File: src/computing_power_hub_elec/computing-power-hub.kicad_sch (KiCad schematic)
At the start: 0 parts

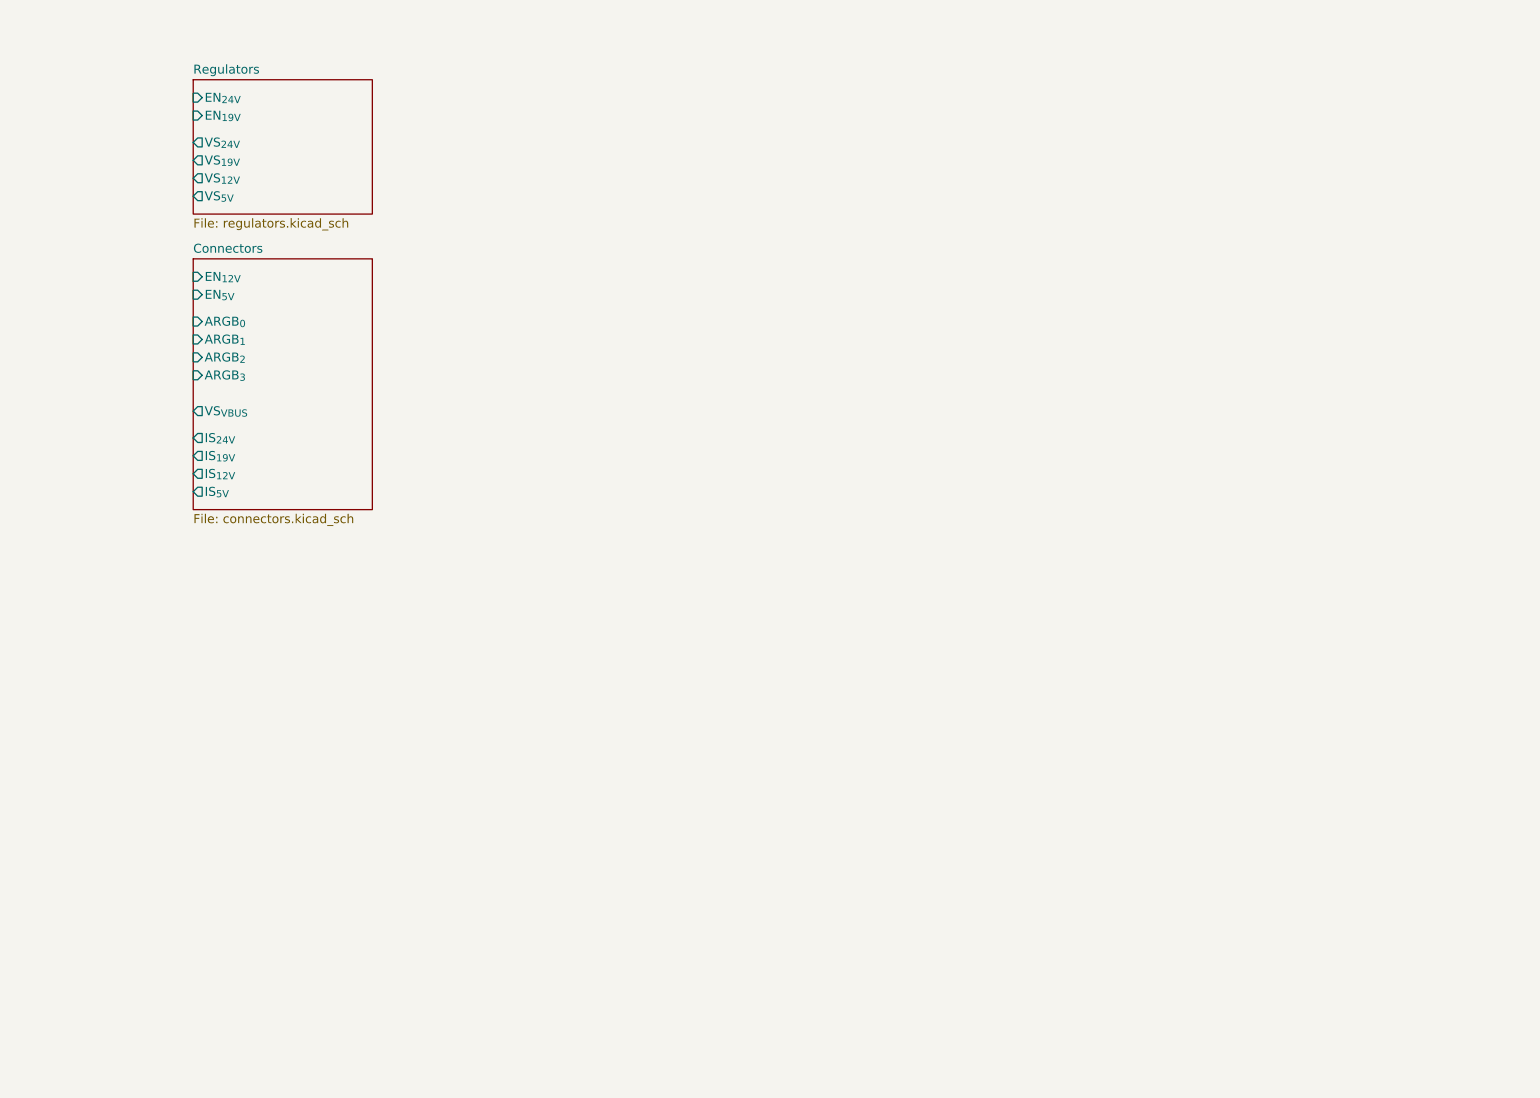
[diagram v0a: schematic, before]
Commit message: Complete first draft of compute power schematic
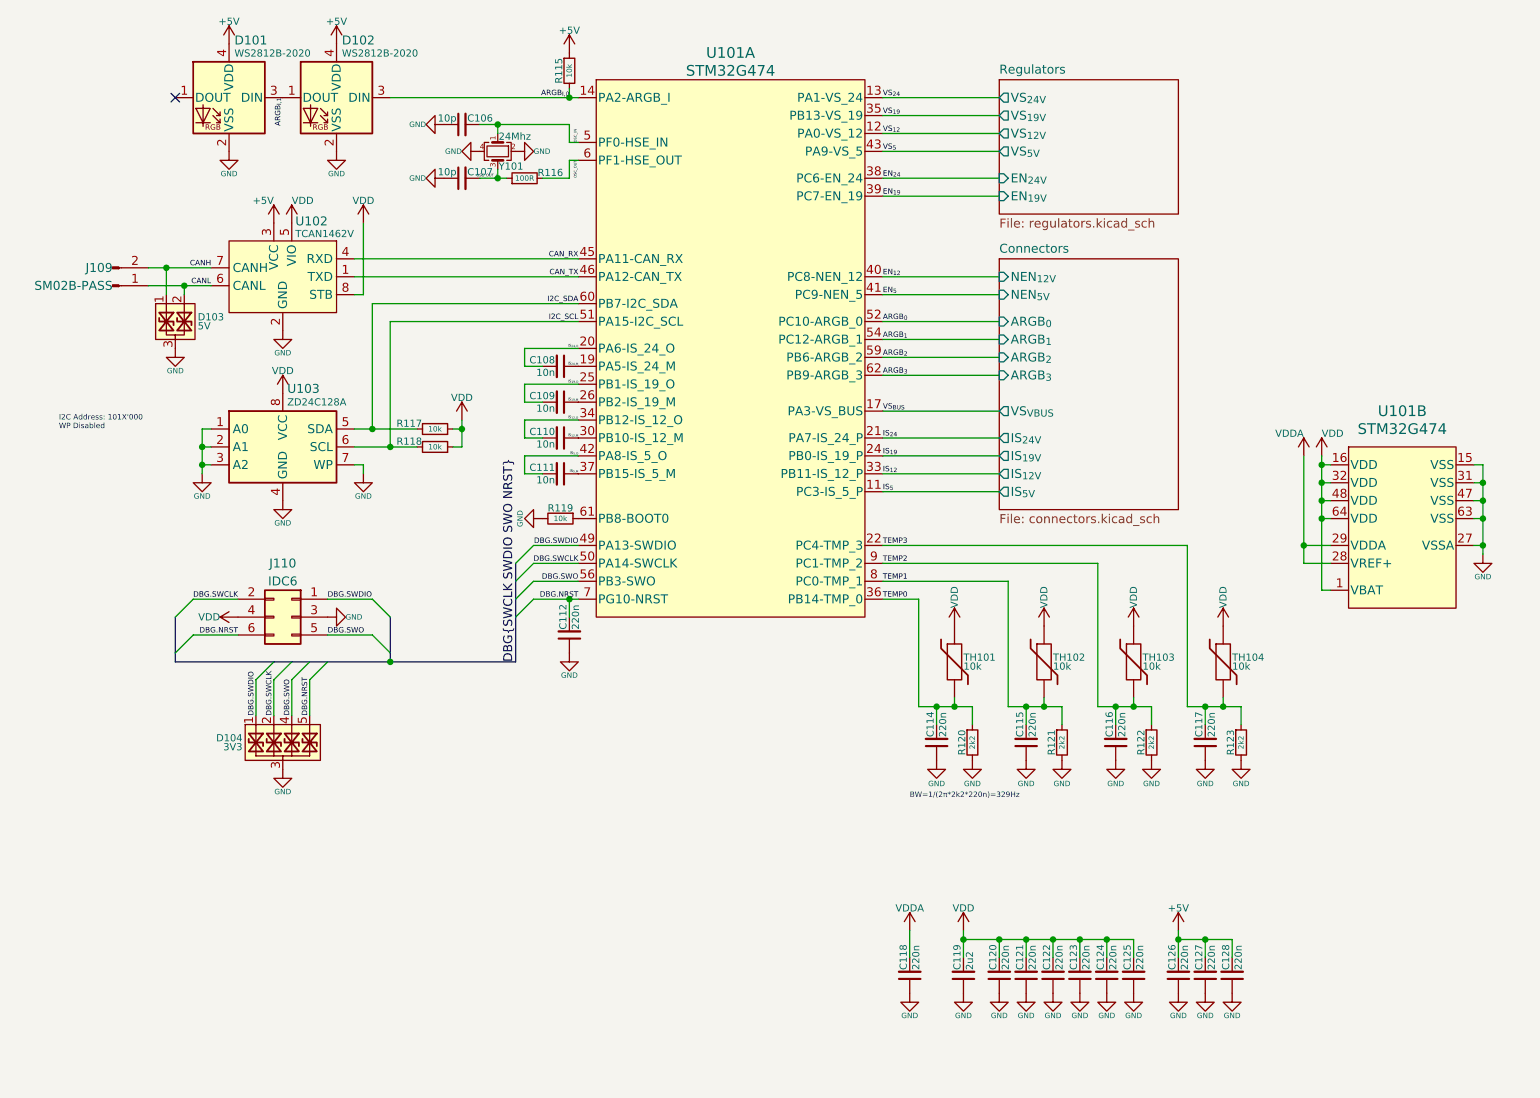
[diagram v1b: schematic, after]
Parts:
- added C106, C107: 10p, Capacitor_SMD:C_0402_1005Metric, symbol Bluesat:C_CompactH
- added C108, C109, C110, C111: 10n, symbol Bluesat:C_CompactV
- added C112, C114, C115, C116, C117, C118, C120, C121, C122, C123, C124, C125, C126, C127, C128: 220n, Capacitor_SMD:C_0402_1005Metric, symbol Bluesat:C_CompactV
- added C119: 2u2, Capacitor_SMD:C_0402_1005Metric, symbol Bluesat:C_CompactV
- added D101, D102: WS2812B-2020, LED_SMD:LED_WS2812B-2020_PLCC4_2.0x2.0mm, symbol LED:WS2812B-2020
- added D103: 5V, Package_TO_SOT_SMD:SOT-523, symbol Bluesat:D_TVS_Dual_Compact
- added D104: 3V3, Package_DFN_QFN:Diodes_UDFN-10_1.0x2.5mm_P0.5mm, symbol Bluesat:D_TVS_Quad_Compact
- added J109: SM02B-PASS, Bluesat:SM02B-PASS, symbol Connector:Conn_01x02_Pin
- added J110: IDC6, Bluesat:IDC6, symbol Connector_Generic:Conn_02x03_Odd_Even
- added R115: 10k, Resistor_SMD:R_0402_1005Metric, symbol Bluesat:R_CompactV
- added R116: 100R, Resistor_SMD:R_0402_1005Metric, symbol Bluesat:R_CompactH
- added R117, R118: 10k, Resistor_SMD:R_0402_1005Metric, symbol Bluesat:R_CompactH
- added R119: 10k, symbol Bluesat:R_CompactV
- added R120, R121, R122, R123: 2k2, Resistor_SMD:R_0402_1005Metric, symbol Bluesat:R_CompactV
- added TH101, TH102, TH103, TH104: 10k, Resistor_SMD:R_0402_1005Metric, symbol Device:Thermistor
- added U101: STM32G474, LQFP64-10x10mm, symbol Bluesat:STM32G474_ComputePower
- added U102: TCAN1462V, symbol Bluesat:TCAN1462V
- added U103: ZD24C128A, Package_SO:TSSOP-8_4.4x3mm_P0.65mm, symbol Memory_EEPROM:24LC128
- added Y101: 24Mhz, Crystal:Crystal_SMD_2016-4Pin_2.0x1.6mm, symbol Device:Crystal_GND24_Small
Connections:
- new net: R119.1, U101.61 (PB8-BOOT0)
- new net +5V: C126.2, C127.2, C128.2, D101.4 (VDD), D102.4 (VDD), R115.1, U102.3 (VCC)
- new net ARGB_{0}: U101.52 (PC10-ARGB_0)
- new net ARGB_{1}: U101.54 (PC12-ARGB_1)
- new net ARGB_{2}: U101.59 (PB6-ARGB_2)
- new net ARGB_{3}: U101.62 (PB9-ARGB_3)
- new net ARGB_{I,0}: D102.3 (DIN), R115.2, U101.14 (PA2-ARGB_I)
- new net ARGB_{I,1}: D101.3 (DIN), D102.1 (DOUT)
- new net CANH: D103.1, J109.2 (Pin_2), U102.7 (CANH)
- new net CANL: D103.2, J109.1 (Pin_1), U102.6 (CANL)
- new net CAN_RX: U101.45 (PA11-CAN_RX), U102.4 (RXD)
- new net CAN_TX: U101.46 (PA12-CAN_TX), U102.1 (TXD)
- new net DBG.NRST: C112.2, D104.5, D104.6, J110.6 (Pin_6), U101.7 (PG10-NRST)
- new net DBG.SWCLK: D104.2, D104.9, J110.2 (Pin_2), U101.50 (PA14-SWCLK)
- new net DBG.SWDIO: D104.1, D104.10, J110.1 (Pin_1), U101.49 (PA13-SWDIO)
- new net DBG.SWO: D104.4, D104.7, J110.5 (Pin_5), U101.56 (PB3-SWO)
- new net EN_{12}: U101.40 (PC8-NEN_12)
- new net EN_{19}: U101.39 (PC7-EN_19)
- new net EN_{24}: U101.38 (PC6-EN_24)
- new net EN_{5}: U101.41 (PC9-NEN_5)
- new net GND: C106.1, C107.1, C112.1, C114.1, C115.1, C116.1, C117.1, C118.1, C119.1, C120.1, C121.1, C122.1, C123.1, C124.1, C125.1, C126.1, C127.1, C128.1, D101.2 (VSS), D102.2 (VSS), D103.3, D104.3, D104.8, J110.3 (Pin_3), R119.2, R120.2, R121.2, R122.2, R123.2, U101.15 (VSS), U101.27 (VSSA), U101.31 (VSS), U101.47 (VSS), U101.63 (VSS), U102.2 (GND), U102.9 (EP), U103.1 (A0), U103.2 (A1), U103.3 (A2), U103.4 (GND), U103.7 (WP), Y101.2, Y101.4
- new net I2C_SCL: R118.2, U101.51 (PA15-I2C_SCL), U103.6 (SCL)
- new net I2C_SDA: R117.2, U101.60 (PB7-I2C_SDA), U103.5 (SDA)
- new net IS_{12,M}: C110.1, U101.30 (PB10-IS_12_M)
- new net IS_{12,O}: C110.2, U101.34 (PB12-IS_12_O)
- new net IS_{12}: U101.33 (PB11-IS_12_P)
- new net IS_{19,M}: C109.1, U101.26 (PB2-IS_19_M)
- new net IS_{19,O}: C109.2, U101.25 (PB1-IS_19_O)
- new net IS_{19}: U101.24 (PB0-IS_19_P)
- new net IS_{24,M}: C108.1, U101.19 (PA5-IS_24_M)
- new net IS_{24,O}: C108.2, U101.20 (PA6-IS_24_O)
- new net IS_{24}: U101.21 (PA7-IS_24_P)
- new net IS_{5,M}: C111.1, U101.37 (PB15-IS_5_M)
- new net IS_{5,O}: C111.2, U101.42 (PA8-IS_5_O)
- new net IS_{5}: U101.11 (PC3-IS_5_P)
- new net OSC_IN: C106.2, U101.5 (PF0-HSE_IN), Y101.1
- new net OSC_OUT: R116.2, U101.6 (PF1-HSE_OUT)
- new net OSC_OUT_L: C107.2, R116.1, Y101.3
- new net TEMP0: C114.2, R120.1, TH101.2, U101.36 (PB14-TMP_0)
- new net TEMP1: C115.2, R121.1, TH102.2, U101.8 (PC0-TMP_1)
- new net TEMP2: C116.2, R122.1, TH103.2, U101.9 (PC1-TMP_2)
- new net TEMP3: C117.2, R123.1, TH104.2, U101.22 (PC4-TMP_3)
- new net VDD: C119.2, C120.2, C121.2, C122.2, C123.2, C124.2, C125.2, J110.4 (Pin_4), R117.1, R118.1, TH101.1, TH102.1, TH103.1, TH104.1, U101.1 (VBAT), U101.16 (VDD), U101.32 (VDD), U101.48 (VDD), U101.64 (VDD), U102.5 (VIO), U102.8 (STB), U103.8 (VCC)
- new net VDDA: C118.2, U101.28 (VREF+), U101.29 (VDDA)
- new net VS_{12}: U101.12 (PA0-VS_12)
- new net VS_{19}: U101.35 (PB13-VS_19)
- new net VS_{24}: U101.13 (PA1-VS_24)
- new net VS_{5}: U101.43 (PA9-VS_5)
- new net VS_{BUS}: U101.17 (PA3-VS_BUS)
- no-connect marks 0 -> 1
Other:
- sheet Connectors ports: added NEN_{12V}, NEN_{5V}; removed EN_{12V}, EN_{5V}
- note added: "BW=1/(2π*2k2*220n)=329Hz"
- note added: "I2C Address: 101X'000 WP Disabled"

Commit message: Is sisyphus happy?
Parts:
- added R101: 10k, Resistor_SMD:R_0402_1005Metric, symbol Bluesat:R_CompactV
- C108, C109, C110, C111: value 10n -> 3n3; footprint (none) -> Capacitor_SMD:C_0402_1005Metric
- C119: footprint Capacitor_SMD:C_0402_1005Metric -> Capacitor_SMD:C_0603_1608Metric
- R119: footprint (none) -> Resistor_SMD:R_0402_1005Metric
- U101: footprint LQFP64-10x10mm -> Package_QFP:LQFP-64_10x10mm_P0.5mm
- U102: footprint (none) -> Package_SO:SOIC-8_3.9x4.9mm_P1.27mm
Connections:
- net DBG.SWCLK: now also R101.1
- net GND: now also R101.2
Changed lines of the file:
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@@
 	)
 	(bus_entry
+		(at 106.68 107.95)
+		(size 2.54 2.54)
+		(stroke
+			(width 0)
+			(type default)
+		)
+	)
+	(bus_entry
 		(at 121.92 99.06)
 		(size 2.54 -2.54)
@@
 	(bus
 		(pts
-			(xy 104.14 107.95) (xy 121.92 107.95)
+			(xy 104.14 107.95) (xy 106.68 107.95)
 		)
 		(stroke
@@
 	(wire
 		(pts
+			(xy 109.22 110.49) (xy 109.22 111.76)
+		)
+		(stroke
+			(width 0)
+			(type default)
+		)
+	)
+	(wire
+		(pts
 			(xy 124.46 91.44) (xy 130.81 91.44)
 		)
@@
 		)
 	)
+	(bus
+		(pts
+			(xy 106.68 107.95) (xy 121.92 107.95)
+		)
+		(stroke
+			(width 0)
+			(type default)
+		)
+	)
 	(wire
 		(pts
@@
 		)
 	)
+	(label "DBG.SWCLK"
+		(at 109.22 110.49 0)
+		(effects
+			(font
+				(size 0.762 0.762)
+			)
+			(justify left bottom)
+		)
+	)
 	(label "ARGB_{I,1}"
 		(at 88.9 27.94 270)
@@
 			)
 		)
-		(property "Footprint" ""
+		(property "Footprint" "Resistor_SMD:R_0402_1005Metric"
 			(at 128.27 87.63 0)
 			(effects
@@
 			)
 		)
-		(property "Footprint" "Capacitor_SMD:C_0402_1005Metric"
+		(property "Footprint" "Capacitor_SMD:C_0603_1608Metric"
 			(at 185.42 152.4 90)
 			(effects
@@
 			)
 		)
-		(property "Value" "10n"
+		(property "Value" "3n3"
 			(at 127.508 72.009 90)
 			(do_not_autoplace yes)
@@
 			)
 		)
-		(property "Footprint" ""
+		(property "Footprint" "Capacitor_SMD:C_0402_1005Metric"
 			(at 128.27 71.12 90)
 			(effects
@@
 	)
 	(symbol
+		(lib_id "power:GND")
+		(at 109.22 116.84 0)
+		(unit 1)
+		(exclude_from_sim no)
+		(in_bom yes)
+		(on_board yes)
+		(dnp no)
+		(property "Reference" "#PWR0240"
+			(at 109.22 123.19 0)
+			(effects
+				(font
+					(size 1.27 1.27)
+				)
+				(hide yes)
+			)
+		)
+		(property "Value" "GND"
+			(at 109.22 120.015 0)
+			(effects
+				(font
+					(size 0.762 0.762)
+				)
+			)
+		)
+		(property "Footprint" ""
+			(at 109.22 116.84 0)
+			(effects
+				(font
+					(size 1.27 1.27)
+				)
+				(hide yes)
+			)
+		)
+		(property "Datasheet" ""
+			(at 109.22 116.84 0)
+			(effects
+				(font
+					(size 1.27 1.27)
+				)
+				(hide yes)
+			)
+		)
+		(property "Description" "Power symbol creates a global label with name \"GND\" , ground"
+			(at 109.22 116.84 0)
+			(effects
+				(font
+					(size 1.27 1.27)
+				)
+				(hide yes)
+			)
+		)
+		(pin "1"
+		)
+		(instances
+			(project "computing-power-hub"
+				(path "/294cc751-7444-4d80-b629-85aa96521600"
+					(reference "#PWR0240")
+					(unit 1)
+				)
+			)
+		)
+	)
+	(symbol
 		(lib_id "Bluesat:C_CompactV")
 		(at 215.9 152.4 0)
@@
 			)
 		)
-		(property "Value" "10n"
+		(property "Value" "3n3"
 			(at 127.508 66.929 90)
 			(do_not_autoplace yes)
@@
 			)
 		)
-		(property "Footprint" ""
+		(property "Footprint" "Capacitor_SMD:C_0402_1005Metric"
 			(at 128.27 66.04 90)
 			(effects
@@
 			)
 		)
-		(property "Footprint" "LQFP64-10x10mm"
+		(property "Footprint" "Package_QFP:LQFP-64_10x10mm_P0.5mm"
 			(at 247.65 77.47 0)
 			(effects
@@
 			)
 		)
-		(property "Value" "10n"
+		(property "Value" "3n3"
 			(at 127.508 82.169 90)
 			(do_not_autoplace yes)
@@
 			)
 		)
-		(property "Footprint" ""
+		(property "Footprint" "Capacitor_SMD:C_0402_1005Metric"
 			(at 128.27 81.28 90)
 			(effects
@@
 	)
 	(symbol
+		(lib_id "Bluesat:R_CompactV")
+		(at 109.22 114.3 0)
+		(unit 1)
+		(exclude_from_sim no)
+		(in_bom yes)
+		(on_board yes)
+		(dnp no)
+		(fields_autoplaced yes)
+		(property "Reference" "R101"
+			(at 108.331 114.3 90)
+			(do_not_autoplace yes)
+			(effects
+				(font
+					(size 1.016 1.016)
+				)
+				(justify bottom)
+			)
+		)
+		(property "Value" "10k"
+			(at 109.22 114.3 90)
+			(do_not_autoplace yes)
+			(effects
+				(font
+					(size 0.762 0.762)
+				)
+			)
+		)
+		(property "Footprint" "Resistor_SMD:R_0402_1005Metric"
+			(at 109.22 114.3 0)
+			(effects
+				(font
+					(size 1.27 1.27)
+				)
+				(hide yes)
+			)
+		)
+		(property "Datasheet" "~"
+			(at 109.22 114.3 0)
+			(effects
+				(font
+					(size 1.27 1.27)
+				)
+				(hide yes)
+			)
+		)
+		(property "Description" "Resistor, compact symbol"
+			(at 109.22 114.3 0)
+			(effects
+				(font
+					(size 1.27 1.27)
+				)
+				(hide yes)
+			)
+		)
+		(pin "1"
+		)
+		(pin "2"
+		)
+		(instances
+			(project "computing-power-hub"
+				(path "/294cc751-7444-4d80-b629-85aa96521600"
+					(reference "R101")
+					(unit 1)
+				)
+			)
+		)
+	)
+	(symbol
 		(lib_id "power:GND")
 		(at 111.76 31.75 270)
@@
 			)
 		)
-		(property "Footprint" ""
+		(property "Footprint" "Package_SO:SOIC-8_3.9x4.9mm_P1.27mm"
 			(at 88.9 53.34 0)
 			(effects
@@
 			)
 		)
-		(property "Value" "10n"
+		(property "Value" "3n3"
 			(at 127.508 77.089 90)
 			(do_not_autoplace yes)
@@
 			)
 		)
-		(property "Footprint" ""
+		(property "Footprint" "Capacitor_SMD:C_0402_1005Metric"
 			(at 128.27 76.2 90)
 			(effects
@@
 			)
 		)
-		(property "Footprint" "LQFP64-10x10mm"
+		(property "Footprint" "Package_QFP:LQFP-64_10x10mm_P0.5mm"
 			(at 152.4 25.4 0)
 			(effects

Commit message: tmp
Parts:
- added R102: 10k, Resistor_SMD:R_0402_1005Metric, symbol Bluesat:R_CompactV
- C112: value 220n -> 10n
- R115: value 10k -> 1k
- R116: value 100R -> 470R
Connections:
- net DBG.NRST: now also J110.5 (Pin_5); no longer J110.6 (Pin_6)
- net DBG.SWCLK: now also J110.1 (Pin_1); no longer J110.2 (Pin_2)
- net DBG.SWDIO: now also J110.2 (Pin_2), R102.1; no longer J110.1 (Pin_1)
- net DBG.SWO: now also J110.6 (Pin_6); no longer J110.5 (Pin_5)
- net GND: now also J110.4 (Pin_4); no longer J110.3 (Pin_3)
- net VDD: now also J110.3 (Pin_3), R102.2; no longer J110.4 (Pin_4)
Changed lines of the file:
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@@
 	)
 	(bus_entry
+		(at 106.68 107.95)
+		(size 2.54 -2.54)
+		(stroke
+			(width 0)
+			(type default)
+		)
+	)
+	(bus_entry
 		(at 76.2 104.14)
 		(size -2.54 2.54)
@@
 	(wire
 		(pts
+			(xy 109.22 105.41) (xy 109.22 104.14)
+		)
+		(stroke
+			(width 0)
+			(type default)
+		)
+	)
+	(wire
+		(pts
 			(xy 219.71 114.3) (xy 222.25 114.3)
 		)
@@
 	(wire
 		(pts
+			(xy 95.25 104.14) (xy 101.6 104.14)
+		)
+		(stroke
+			(width 0)
+			(type default)
+		)
+	)
+	(wire
+		(pts
 			(xy 173.99 81.28) (xy 190.5 81.28)
 		)
@@
 	(wire
 		(pts
-			(xy 101.6 99.06) (xy 95.25 99.06)
-		)
-		(stroke
-			(width 0)
-			(type default)
-		)
-	)
-	(wire
-		(pts
 			(xy 205.74 149.86) (xy 205.74 147.32)
 		)
@@
 	(wire
 		(pts
+			(xy 95.25 99.06) (xy 101.6 99.06)
+		)
+		(stroke
+			(width 0)
+			(type default)
+		)
+	)
+	(wire
+		(pts
 			(xy 236.22 85.09) (xy 237.49 85.09)
 		)
@@
 	(wire
 		(pts
-			(xy 101.6 104.14) (xy 95.25 104.14)
-		)
-		(stroke
-			(width 0)
-			(type default)
-		)
-	)
-	(wire
-		(pts
 			(xy 236.22 78.74) (xy 236.22 80.01)
 		)
@@
 		)
 	)
+	(label "DBG.SWDIO"
+		(at 109.22 105.41 0)
+		(effects
+			(font
+				(size 0.762 0.762)
+			)
+			(justify left bottom)
+		)
+	)
 	(label "DBG.NRST"
 		(at 92.71 115.57 90)
@@
 			)
 		)
-		(property "Value" "10k"
+		(property "Value" "1k"
 			(at 129.54 24.13 90)
 			(do_not_autoplace yes)
@@
 	(symbol
 		(lib_id "Connector_Generic:Conn_02x03_Odd_Even")
-		(at 90.17 101.6 0)
-		(mirror y)
+		(at 87.63 101.6 0)
 		(unit 1)
 		(exclude_from_sim no)
@@
 		)
 		(property "Footprint" "Bluesat:IDC6"
-			(at 90.17 101.6 0)
+			(at 87.63 101.6 0)
 			(effects
 				(font
@@
 		)
 		(property "Datasheet" "~"
-			(at 90.17 101.6 0)
+			(at 87.63 101.6 0)
 			(effects
 				(font
@@
 		)
 		(property "Description" "Generic connector, double row, 02x03, odd/even pin numbering scheme (row 1 odd numbers, row 2 even numbers), script generated (kicad-library-utils/schlib/autogen/connector/)"
-			(at 90.17 101.6 0)
+			(at 87.63 101.6 0)
 			(effects
 				(font
@@
 	)
 	(symbol
+		(lib_id "power:VDD")
+		(at 109.22 99.06 0)
+		(mirror y)
+		(unit 1)
+		(exclude_from_sim no)
+		(in_bom yes)
+		(on_board yes)
+		(dnp no)
+		(property "Reference" "#PWR0101"
+			(at 109.22 102.87 0)
+			(effects
+				(font
+					(size 1.27 1.27)
+				)
+				(hide yes)
+			)
+		)
+		(property "Value" "VDD"
+			(at 109.22 95.885 0)
+			(effects
+				(font
+					(size 1.016 1.016)
+				)
+			)
+		)
+		(property "Footprint" ""
+			(at 109.22 99.06 0)
+			(effects
+				(font
+					(size 1.27 1.27)
+				)
+				(hide yes)
+			)
+		)
+		(property "Datasheet" ""
+			(at 109.22 99.06 0)
+			(effects
+				(font
+					(size 1.27 1.27)
+				)
+				(hide yes)
+			)
+		)
+		(property "Description" "Power symbol creates a global label with name \"VDD\""
+			(at 109.22 99.06 0)
+			(effects
+				(font
+					(size 1.27 1.27)
+				)
+				(hide yes)
+			)
+		)
+		(pin "1"
+		)
+		(instances
+			(project "computing-power-hub"
+				(path "/294cc751-7444-4d80-b629-85aa96521600"
+					(reference "#PWR0101")
+					(unit 1)
+				)
+			)
+		)
+	)
+	(symbol
+		(lib_id "Bluesat:R_CompactV")
+		(at 109.22 101.6 0)
+		(mirror x)
+		(unit 1)
+		(exclude_from_sim no)
+		(in_bom yes)
+		(on_board yes)
+		(dnp no)
+		(fields_autoplaced yes)
+		(property "Reference" "R102"
+			(at 108.331 101.6 90)
+			(do_not_autoplace yes)
+			(effects
+				(font
+					(size 1.016 1.016)
+				)
+				(justify bottom)
+			)
+		)
+		(property "Value" "10k"
+			(at 109.22 101.6 90)
+			(do_not_autoplace yes)
+			(effects
+				(font
+					(size 0.762 0.762)
+				)
+			)
+		)
+		(property "Footprint" "Resistor_SMD:R_0402_1005Metric"
+			(at 109.22 101.6 0)
+			(effects
+				(font
+					(size 1.27 1.27)
+				)
+				(hide yes)
+			)
+		)
+		(property "Datasheet" "~"
+			(at 109.22 101.6 0)
+			(effects
+				(font
+					(size 1.27 1.27)
+				)
+				(hide yes)
+			)
+		)
+		(property "Description" "Resistor, compact symbol"
+			(at 109.22 101.6 0)
+			(effects
+				(font
+					(size 1.27 1.27)
+				)
+				(hide yes)
+			)
+		)
+		(pin "1"
+		)
+		(pin "2"
+		)
+		(instances
+			(project "computing-power-hub"
+				(path "/294cc751-7444-4d80-b629-85aa96521600"
+					(reference "R102")
+					(unit 1)
+				)
+			)
+		)
+	)
+	(symbol
 		(lib_id "Bluesat:C_CompactV")
 		(at 205.74 152.4 0)
@@
 			)
 		)
-		(property "Value" "220n"
+		(property "Value" "10n"
 			(at 130.429 103.378 90)
 			(do_not_autoplace yes)
@@
 			)
 		)
-		(property "Value" "100R"
+		(property "Value" "470R"
 			(at 123.19 39.37 0)
 			(do_not_autoplace yes)

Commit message: Temp
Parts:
- added C101: 220n, Capacitor_SMD:C_0402_1005Metric, symbol Bluesat:C_CompactV
- added D105: WS2812B-2020, LED_SMD:LED_WS2812B-2020_PLCC4_2.0x2.0mm, symbol LED:WS2812B-2020
- C108, C109, C110, C111: value 3n3 -> 100p
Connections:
- net +5V: now also C101.2, D105.4 (VDD)
- net DBG.NRST: now also J110.2 (Pin_2); no longer J110.5 (Pin_5)
- net DBG.SWCLK: now also J110.6 (Pin_6); no longer J110.1 (Pin_1)
- net DBG.SWDIO: now also J110.5 (Pin_5); no longer J110.2 (Pin_2)
- net DBG.SWO: now also J110.1 (Pin_1); no longer J110.6 (Pin_6)
- net GND: now also C101.1, D105.2 (VSS)
- net ARGB_{I,2}: now reaches D101.1 (DOUT)
- net ARGB_{I,2}: now also D105.3 (DIN)
